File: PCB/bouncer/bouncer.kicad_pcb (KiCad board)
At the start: 2 copper layers, 15 parts, among them J1 Conn_01x08_Female, SW1 SW_Push_Dual, SW2 SW_Push_Dual, SW3 SW_Push_Dual, U1 74HC14

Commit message: Final changes for v2
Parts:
- added ?: MountingHole_3.2mm_M3_DIN965_Pad, MountingHole:MountingHole_3.2mm_M3_DIN965_Pad, F.Cu at (189.6, 118.5)
- added ?: MountingHole_3.2mm_M3_DIN965_Pad, MountingHole:MountingHole_3.2mm_M3_DIN965_Pad, F.Cu at (129.6, 118.5)
- added ?: MountingHole_3.2mm_M3_DIN965_Pad, MountingHole:MountingHole_3.2mm_M3_DIN965_Pad, F.Cu at (190.0, 81.8)
- added ?: MountingHole_3.2mm_M3_DIN965_Pad, MountingHole:MountingHole_3.2mm_M3_DIN965_Pad, F.Cu at (129.6, 81.8)
- moved C4 9.59 mm to (177.6, 98.1), turned to -90 degrees
- moved R1 9.23 mm to (143.0, 105.1)
- moved SW3 8.85 mm to (183.8, 117.1)
- moved R6 8.82 mm to (183.8, 97.7)
- moved R2 8.78 mm to (147.9, 97.9)
- moved SW1 8.75 mm to (147.9, 117.1)
- moved C1 8.30 mm to (141.7, 98.3), turned to -90 degrees
- moved R5 7.86 mm to (179.1, 104.9)
- moved C3 4.78 mm to (147.1, 88.5)
- moved J1 2.53 mm to (149.3, 81.5)
- moved U1 2.27 mm to (151.9, 93.5)
- moved C2 1.16 mm to (159.6, 98.2), turned to -90 degrees
- moved R3 1.07 mm to (161.0, 104.9)
- moved R4 0.14 mm to (165.8, 97.8)
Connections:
- net ~BUTTON_1 renamed ~{BUTTON_1}
- net ~BUTTON_2 renamed ~{BUTTON_2}
- net ~BUTTON_3 renamed ~{BUTTON_3}
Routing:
- net GND: track 176.1 -> 0.00 mm
- net +5V: track 107.0 -> 70.9 mm
- net Net-(R6-Pad1): track 33.8 -> 23.8 mm
- net Net-(R2-Pad1): track 20.1 -> 12.4 mm
- net Net-(R5-Pad1): track 25.8 -> 24.2 mm
- net Net-(R4-Pad1): track 13.6 -> 12.2 mm
- net ~{BUTTON_3}: track 4.17 -> 5.44 mm
- net ~{BUTTON_2}: track 4.17 -> 5.44 mm
- net BUTTON_2: track 11.8 -> 13.1 mm
- net ~{BUTTON_1}: track 4.17 -> 5.44 mm
- net BUTTON_3: track 11.8 -> 13.1 mm
- net BUTTON_1: track 11.8 -> 13.1 mm
- net Net-(R1-Pad1): track 24.8 -> 24.2 mm
- net Net-(R3-Pad1): track 24.8 -> 24.2 mm
- added copper zone on B.Cu, net GND
- added copper zone on F.Cu, net GND
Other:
- board outline added: 70.1 x 47.1 mm
- net class Default removed
- board text added: "1"
- board text added: "2"
- board text added: "3"
- board text added: "5V"
- board text added: "Button 1"
- board text added: "Button 2"
- board text added: "Button 3"
- board text added: "GND"

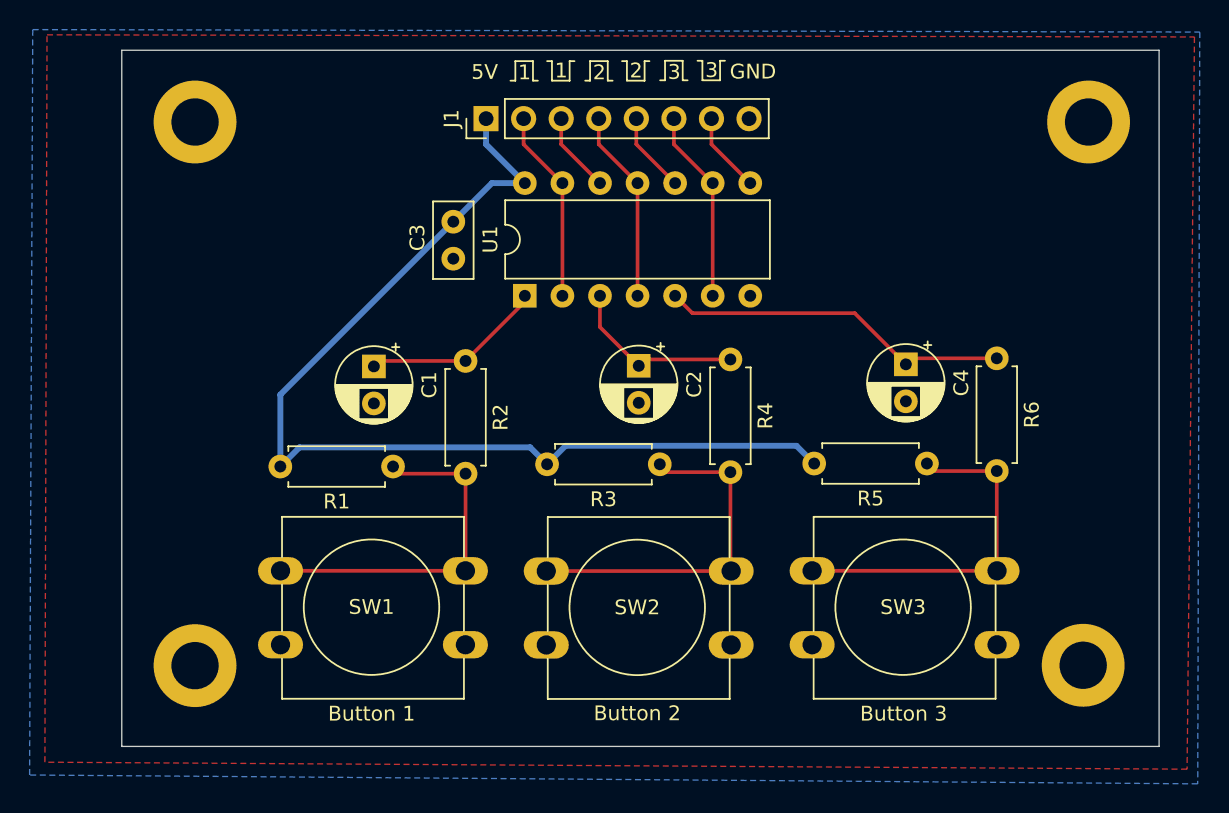
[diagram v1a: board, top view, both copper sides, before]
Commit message: added 2 new soundcard designs
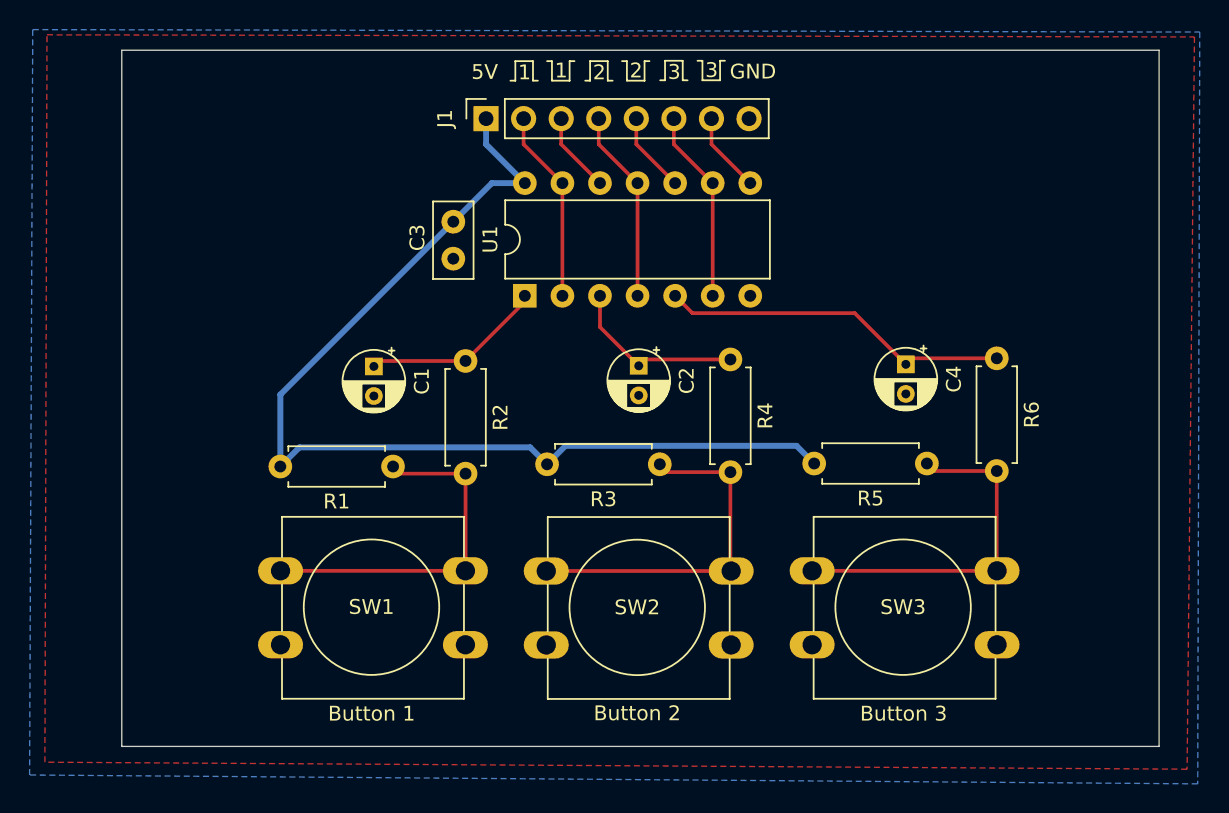
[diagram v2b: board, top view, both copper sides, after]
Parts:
- removed ? (x4): MountingHole_3.2mm_M3_DIN965_Pad, MountingHole:MountingHole_3.2mm_M3_DIN965_Pad
- C1, C2, C4: footprint Capacitor_THT:CP_Radial_D5.0mm_P2.50mm -> Capacitor_THT:CP_Radial_D4.0mm_P2.00mm
- J1: footprint Connector_PinHeader_2.54mm:PinHeader_1x08_P2.54mm_Vertical -> Connector_PinSocket_2.54mm:PinSocket_1x08_P2.54mm_Vertical

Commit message: rc1 for SPI Gate (prev SPI master) rc1 for Bouncer
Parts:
- added H1: MountingHole, MountingHole:MountingHole_3.2mm_M3_DIN965_Pad, F.Cu at (129.0, 81.4)
- added H2: MountingHole, MountingHole:MountingHole_3.2mm_M3_DIN965_Pad, F.Cu at (190.4, 81.4)
- added H3: MountingHole, MountingHole:MountingHole_3.2mm_M3_DIN965_Pad, F.Cu at (129.0, 119.5)
- added H4: MountingHole, MountingHole:MountingHole_3.2mm_M3_DIN965_Pad, F.Cu at (190.4, 119.5)
- moved J1 1.56 mm to (150.8, 81.5)
- moved C3 0.57 mm to (147.6, 88.5)
- moved U1 0.57 mm to (152.5, 93.5)
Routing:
- net +5V: track 70.9 -> 77.0 mm
- net Net-(C1-Pad1): track 12.4 -> 13.2 mm
- net Net-(C4-Pad1): track 23.8 -> 23.3 mm
- net GND: vias 0 -> 1
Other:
- board size 70.1 x 47.1 mm -> 70.1 x 46.9 mm
- board text added: "+5V"
- board text added: "Bouncer"
- board text added: "v1.0 by Nate Rivard Nov 2024"
- board text removed: "5V"

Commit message: Added SpiMaster support
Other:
- board text added: "JLCJLCJLCJLC"
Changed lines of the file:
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@@
 			(outputformat 1)
 			(mirror no)
-			(drillshape 1)
+			(drillshape 0)
 			(scaleselection 1)
-			(outputdirectory "")
+			(outputdirectory "gerbers/")
 		)
 	)
@@
 		(tags "CP Radial series Radial pin pitch 2.00mm  diameter 4mm Electrolytic Capacitor")
 		(property "Reference" "C2"
-			(at 1 -3.25 -90)
+			(at 1.016 -1.4478 -90)
 			(layer "F.SilkS")
 			(effects
@@
 		)
 		(property "Value" "10uF"
-			(at 1 3.25 -90)
-			(layer "F.Fab")
+			(at 1 3.25 270)
+			(layer "F.SilkS")
 			(effects
 				(font
@@
 		(tags "CP Radial series Radial pin pitch 2.00mm  diameter 4mm Electrolytic Capacitor")
 		(property "Reference" "C4"
-			(at 1 -3.25 -90)
+			(at 1 -1.4732 -90)
 			(layer "F.SilkS")
 			(effects
@@
 		)
 		(property "Value" "10uF"
-			(at 1 3.25 -90)
-			(layer "F.Fab")
+			(at 1 3.25 270)
+			(layer "F.SilkS")
 			(effects
 				(font
@@
 		(tags "Resistor Axial_DIN0207 series Axial Horizontal pin pitch 7.62mm 0.25W = 1/4W length 6.3mm diameter 2.5mm")
 		(property "Reference" "R1"
-			(at 3.81 -2.37 0)
+			(at 3.7846 0 0)
 			(layer "F.SilkS")
 			(effects
@@
 		(property "Value" "2K"
 			(at 3.81 2.37 0)
-			(layer "F.Fab")
+			(layer "F.SilkS")
 			(effects
 				(font
@@
 		(tags "Resistor Axial_DIN0207 series Axial Horizontal pin pitch 7.62mm 0.25W = 1/4W length 6.3mm diameter 2.5mm")
 		(property "Reference" "R2"
-			(at 3.81 -2.37 90)
+			(at 3.81 -0.0508 90)
 			(layer "F.SilkS")
 			(effects
@@
 		(property "Value" "560R"
 			(at 3.81 2.37 90)
-			(layer "F.Fab")
+			(layer "F.SilkS")
 			(effects
 				(font
@@
 		(tags "THT DIP DIL PDIP 2.54mm 7.62mm 300mil")
 		(property "Reference" "U1"
-			(at 3.81 -2.33 90)
+			(at 3.81 1.38684 90)
 			(layer "F.SilkS")
 			(effects
@@
 		(property "Value" "74HC14"
 			(at 3.81 17.57 90)
-			(layer "F.Fab")
+			(layer "F.SilkS")
 			(effects
 				(font
@@
 		(tags "Resistor Axial_DIN0207 series Axial Horizontal pin pitch 7.62mm 0.25W = 1/4W length 6.3mm diameter 2.5mm")
 		(property "Reference" "R5"
-			(at 3.81 -2.37 0)
+			(at 3.81 0 0)
 			(layer "F.SilkS")
 			(effects
@@
 		(property "Value" "2K"
 			(at 3.81 2.37 0)
-			(layer "F.Fab")
+			(layer "F.SilkS")
 			(effects
 				(font
@@
 		(tags "Resistor Axial_DIN0207 series Axial Horizontal pin pitch 7.62mm 0.25W = 1/4W length 6.3mm diameter 2.5mm")
 		(property "Reference" "R3"
-			(at 3.81 -2.37 0)
+			(at 3.7846 0 0)
 			(layer "F.SilkS")
 			(effects
@@
 		(property "Value" "2K"
 			(at 3.81 2.37 0)
-			(layer "F.Fab")
+			(layer "F.SilkS")
 			(effects
 				(font
@@
 			(at 1.07696 2.42316 90)
 			(layer "F.SilkS")
+			(hide yes)
 			(effects
 				(font
@@
 		(property "Value" "100nF"
 			(at 1.25 2.5 90)
-			(layer "F.Fab")
+			(layer "F.SilkS")
 			(effects
 				(font
@@
 		(tags "Resistor Axial_DIN0207 series Axial Horizontal pin pitch 7.62mm 0.25W = 1/4W length 6.3mm diameter 2.5mm")
 		(property "Reference" "R6"
-			(at 3.81 -2.37 90)
+			(at 3.81 0 90)
 			(layer "F.SilkS")
 			(effects
@@
 		(property "Value" "560R"
 			(at 3.81 2.37 90)
-			(layer "F.Fab")
+			(layer "F.SilkS")
 			(effects
 				(font
@@
 		(tags "Resistor Axial_DIN0207 series Axial Horizontal pin pitch 7.62mm 0.25W = 1/4W length 6.3mm diameter 2.5mm")
 		(property "Reference" "R4"
-			(at 3.81 -2.37 90)
+			(at 3.7338 0.0254 90)
 			(layer "F.SilkS")
 			(effects
@@
 		(property "Value" "560R"
 			(at 3.81 2.37 90)
-			(layer "F.Fab")
+			(layer "F.SilkS")
 			(effects
 				(font
@@
 		(tags "CP Radial series Radial pin pitch 2.00mm  diameter 4mm Electrolytic Capacitor")
 		(property "Reference" "C1"
-			(at 1 -3.25 -90)
+			(at 1.027313 -1.4224 -90)
 			(layer "F.SilkS")
 			(effects
@@
 		)
 		(property "Value" "10uF"
-			(at 1 3.25 -90)
-			(layer "F.Fab")
+			(at 1 3.25 270)
+			(layer "F.SilkS")
 			(effects
 				(font
@@
 		)
 	)
+	(gr_text "JLCJLCJLCJLC"
+		(at 156.3624 90.2716 0)
+		(layer "F.SilkS")
+		(effects
+			(font
+				(size 0.8 0.8)
+				(thickness 0.15)
+			)
+			(justify left bottom)
+		)
+	)
